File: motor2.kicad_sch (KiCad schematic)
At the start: 58 parts, among them IC3 DRV8300DPWR, IC4 DRV8300DPWR, J1 Conn_01x01, J2 Conn_01x01, J3 Conn_01x01, J4 Conn_01x01, J5 Conn_01x01, J6 Conn_01x01, Q1 Q_NMOS, Q10 Q_NMOS, Q11 Q_NMOS, Q12 Q_NMOS, Q2 Q_NMOS, Q3 Q_NMOS, Q4 Q_NMOS, Q5 Q_NMOS, Q6 Q_NMOS, Q7 Q_NMOS, Q8 Q_NMOS, Q9 Q_NMOS

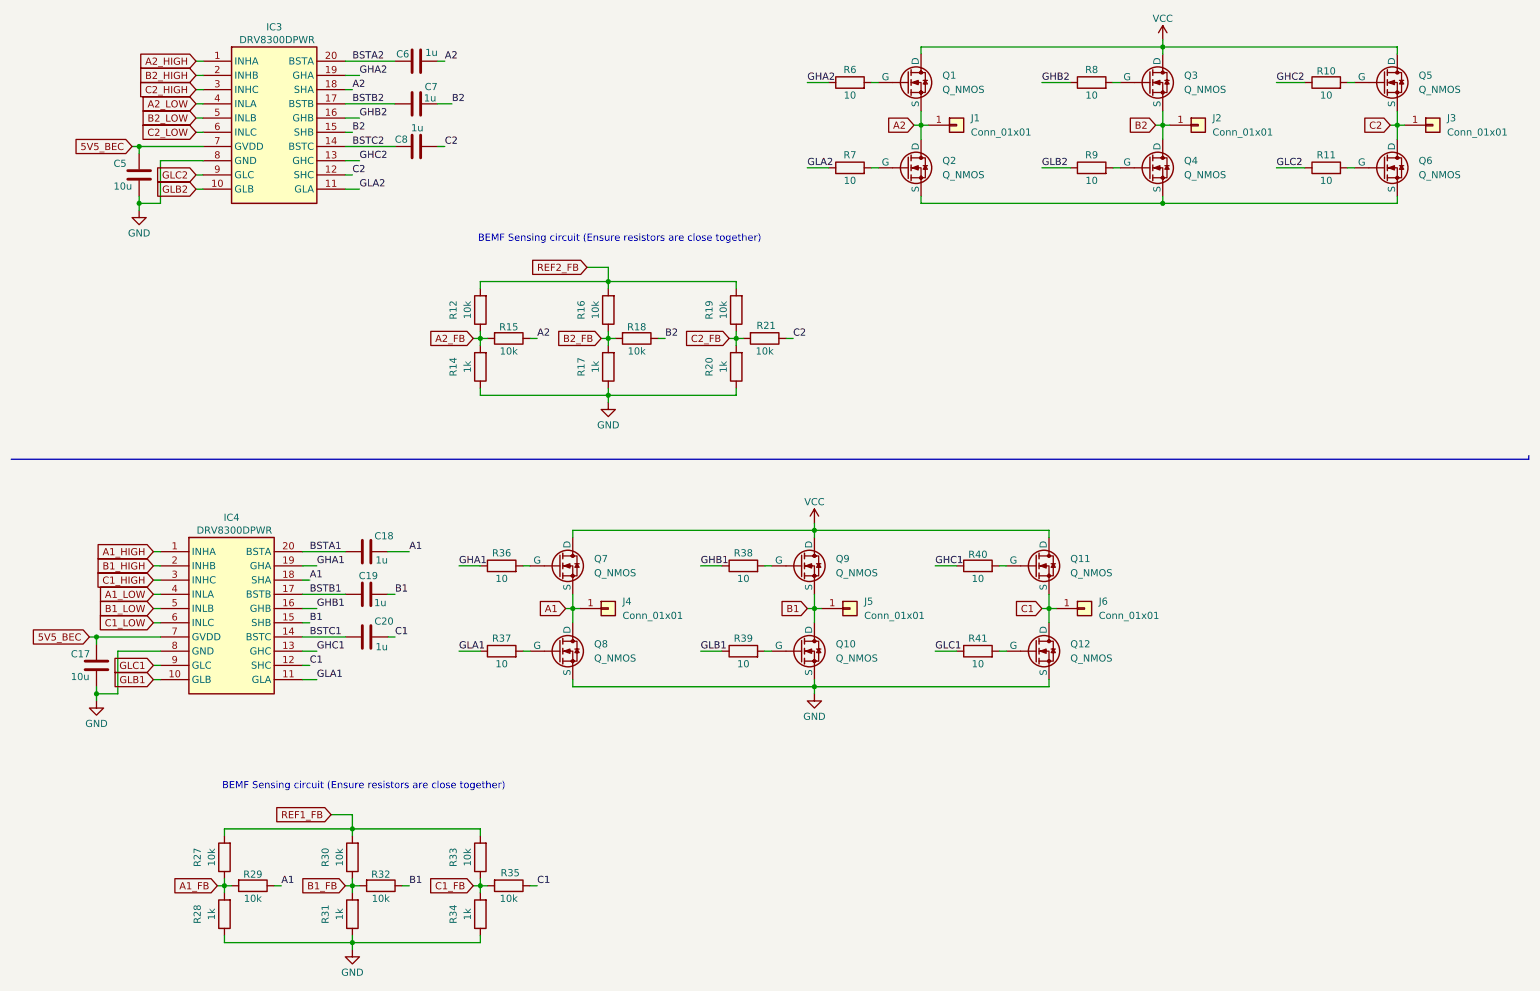
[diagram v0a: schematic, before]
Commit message: update schematic
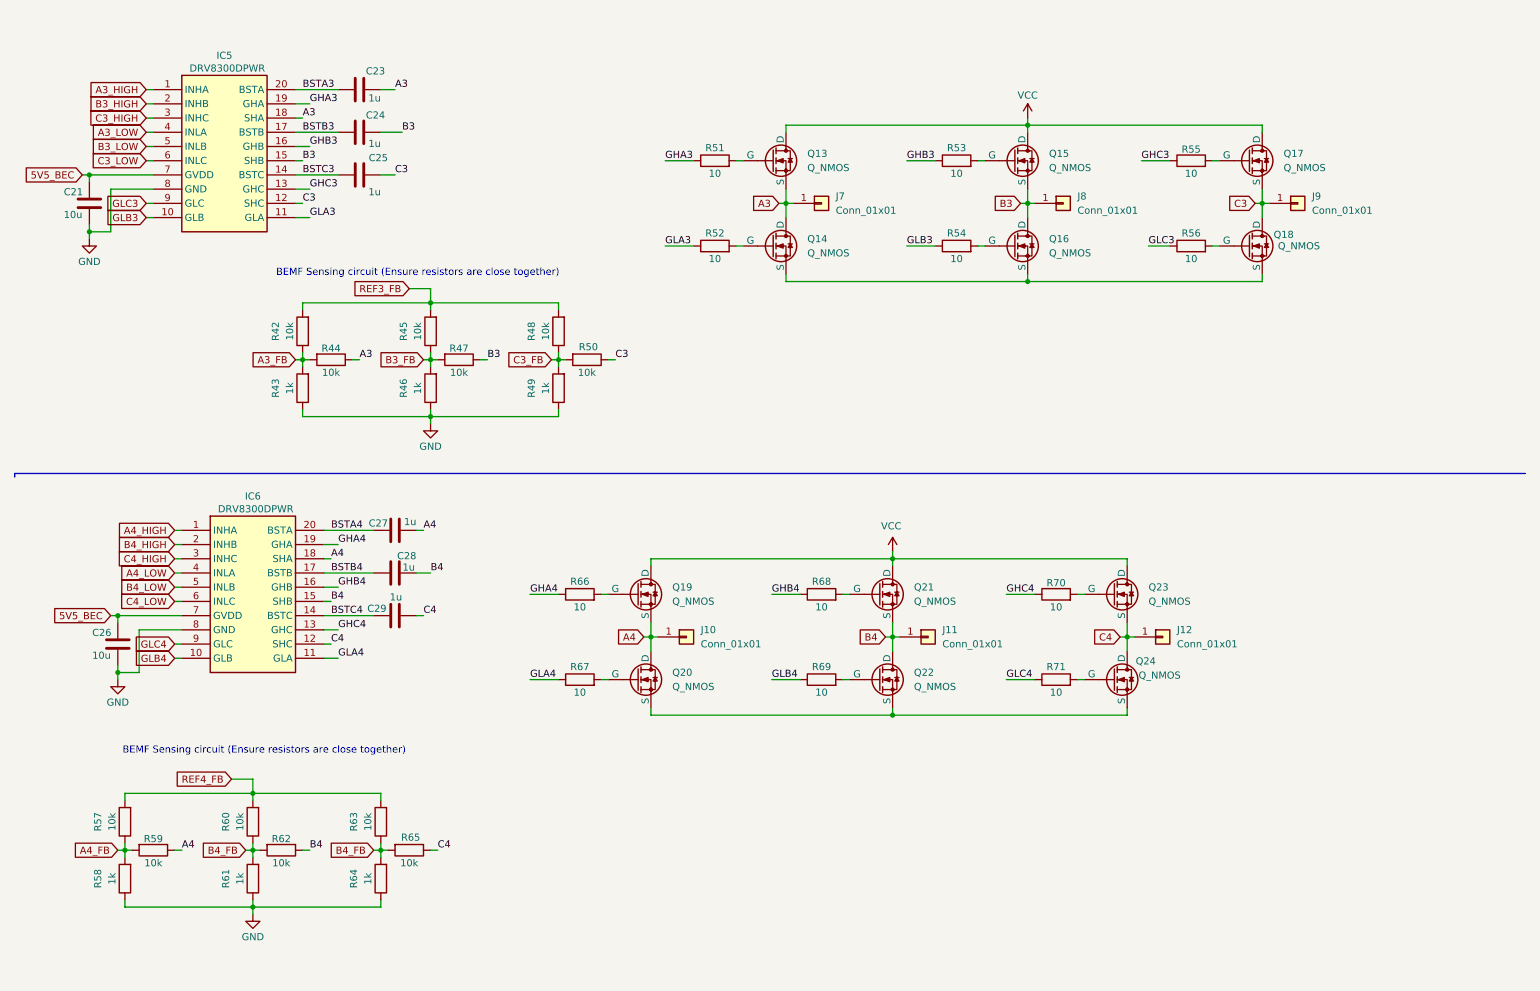
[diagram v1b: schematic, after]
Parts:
- removed C17, C5: 10u, symbol Device:C
- removed C18, C19, C20, C6, C7, C8: 1u, symbol Device:C
- removed IC3, IC4: DRV8300DPWR, ESCs:SOP65P640X120-20M, symbol ESCs:DRV8300DPWR
- removed J1, J2, J3, J4, J5, J6: Conn_01x01, symbol Connector_Generic:Conn_01x01
- removed Q1, Q10, Q11, Q12, Q2, Q3, Q4, Q5, Q6, Q7, Q8, Q9: Q_NMOS, symbol Device:Q_NMOS
- removed R10, R11, R36, R37, R38, R39, R40, R41, R6, R7, R8, R9: 10, symbol Device:R
- removed R12, R15, R16, R18, R19, R21, R27, R29, R30, R32, R33, R35: 10k, symbol Device:R
- removed R14, R17, R20, R28, R31, R34: 1k, symbol Device:R
- added C21, C26: 10u, symbol Device:C
- added C23, C24, C25, C27, C28, C29: 1u, symbol Device:C
- added IC5, IC6: DRV8300DPWR, ESCs:SOP65P640X120-20M, symbol ESCs:DRV8300DPWR
- added J10, J11, J12, J7, J8, J9: Conn_01x01, symbol Connector_Generic:Conn_01x01
- added Q13, Q14, Q15, Q16, Q17, Q18, Q19, Q20, Q21, Q22, Q23, Q24: Q_NMOS, symbol Device:Q_NMOS
- added R42, R44, R45, R47, R48, R50, R57, R59, R60, R62, R63, R65: 10k, symbol Device:R
- added R43, R46, R49, R58, R61, R64: 1k, symbol Device:R
- added R51, R52, R53, R54, R55, R56, R66, R67, R68, R69, R70, R71: 10, symbol Device:R
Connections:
- net 5V5_BEC: now also C21.1, C26.1, IC5.7 (GVDD), IC6.7 (GVDD)
- net GND: now also C21.2, C26.2, IC5.8 (GND), IC6.8 (GND), R43.1, R46.1, R49.1, R58.1, R61.1, R64.1
- net VCC: now also Q13.D, Q15.D, Q17.D, Q19.D, Q21.D, Q23.D
- new net: Q15.G, R53.2
- new net: Q20.G, R67.2
- new net: Q20.S, Q22.S, Q24.S
- new net: Q19.G, R66.2
- new net: Q22.G, R69.2
- new net: Q23.G, R70.2
- new net: Q24.G, R71.2
- new net: Q17.G, R55.2
- new net: Q21.G, R68.2
- new net: Q13.G, R51.2
- new net: Q14.G, R52.2
- new net: Q14.S, Q16.S, Q18.S
- new net: Q18.G, R56.2
- new net: Q16.G, R54.2
- new net A3: C23.2, IC5.18 (SHA), J7.1 (Pin_1), Q13.S, Q14.D, R44.1
- new net A3_FB: R42.1, R43.2, R44.2
- new net A3_HIGH: IC5.1 (INHA)
- new net A3_LOW: IC5.4 (INLA)
- new net A4: C27.2, IC6.18 (SHA), J10.1 (Pin_1), Q19.S, Q20.D, R59.1
- new net A4_FB: R57.1, R58.2, R59.2
- new net A4_HIGH: IC6.1 (INHA)
- new net A4_LOW: IC6.4 (INLA)
- new net B3: C24.2, IC5.15 (SHB), J8.1 (Pin_1), Q15.S, Q16.D, R47.1
- new net B3_FB: R45.1, R46.2, R47.2
- new net B3_HIGH: IC5.2 (INHB)
- new net B3_LOW: IC5.5 (INLB)
- new net B4: C28.2, IC6.15 (SHB), J11.1 (Pin_1), Q21.S, Q22.D, R62.1
- new net B4_FB: R60.1, R61.2, R62.2, R63.1, R64.2, R65.2
- new net B4_HIGH: IC6.2 (INHB)
- new net B4_LOW: IC6.5 (INLB)
- new net BSTA3: C23.1, IC5.20 (BSTA)
- new net BSTA4: C27.1, IC6.20 (BSTA)
- new net BSTB3: C24.1, IC5.17 (BSTB)
- new net BSTB4: C28.1, IC6.17 (BSTB)
- new net BSTC3: C25.1, IC5.14 (BSTC)
- new net BSTC4: C29.1, IC6.14 (BSTC)
- new net C3: C25.2, IC5.12 (SHC), J9.1 (Pin_1), Q17.S, Q18.D, R50.1
- new net C3_FB: R48.1, R49.2, R50.2
- new net C3_HIGH: IC5.3 (INHC)
- new net C3_LOW: IC5.6 (INLC)
- new net C4: C29.2, IC6.12 (SHC), J12.1 (Pin_1), Q23.S, Q24.D, R65.1
- new net C4_HIGH: IC6.3 (INHC)
- new net C4_LOW: IC6.6 (INLC)
- new net GHA3: IC5.19 (GHA), R51.1
- new net GHA4: IC6.19 (GHA), R66.1
- new net GHB3: IC5.16 (GHB), R53.1
- new net GHB4: IC6.16 (GHB), R68.1
- new net GHC3: IC5.13 (GHC), R55.1
- new net GHC4: IC6.13 (GHC), R70.1
- new net GLA3: IC5.11 (GLA), R52.1
- new net GLA4: IC6.11 (GLA), R67.1
- new net GLB3: IC5.10 (GLB), R54.1
- new net GLB4: IC6.10 (GLB), R69.1
- new net GLC3: IC5.9 (GLC), R56.1
- new net GLC4: IC6.9 (GLC), R71.1
- new net REF3_FB: R42.2, R45.2, R48.2
- new net REF4_FB: R57.2, R60.2, R63.2

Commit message: affected footprints
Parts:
- C21, C23, C24, C25, C26, C27, C28, C29: footprint (none) -> Capacitor_SMD:C_0402_1005Metric
- J10, J11, J12, J7, J8, J9: footprint (none) -> TestPoint:TestPoint_Pad_2.0x2.0mm; now left out of the parts list
- Q13, Q14, Q15, Q16, Q17, Q18, Q19, Q20, Q21, Q22, Q23, Q24: footprint (none) -> ESCs:TRANS_NTMFS5C628NLT1G
- R42, R43, R44, R45, R46, R47, R48, R49, R50, R51, R52, R53, R54, R55, R56, R57, R58, R59, R60, R61, R62, R63, R64, R65, R66, R67, R68, R69, R70, R71: footprint (none) -> Resistor_SMD:R_0402_1005Metric
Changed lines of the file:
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@@
 			)
 		)
-		(property "Footprint" ""
+		(property "Footprint" "Resistor_SMD:R_0402_1005Metric"
 			(at 181.61 42.418 90)
 			(effects
@@
 			)
 		)
-		(property "Footprint" ""
+		(property "Footprint" "ESCs:TRANS_NTMFS5C628NLT1G"
 			(at 129.54 130.81 0)
 			(effects
@@
 			)
 		)
-		(property "Footprint" ""
+		(property "Footprint" "ESCs:TRANS_NTMFS5C628NLT1G"
 			(at 129.54 115.57 0)
 			(effects
@@
 			)
 		)
-		(property "Footprint" ""
+		(property "Footprint" "Resistor_SMD:R_0402_1005Metric"
 			(at 66.548 71.12 90)
 			(effects
@@
 			)
 		)
-		(property "Footprint" ""
+		(property "Footprint" "Resistor_SMD:R_0402_1005Metric"
 			(at 112.268 81.28 90)
 			(effects
@@
 			)
 		)
-		(property "Footprint" ""
+		(property "Footprint" "Resistor_SMD:R_0402_1005Metric"
 			(at 157.48 135.128 90)
 			(effects
@@
 			)
 		)
-		(property "Footprint" ""
+		(property "Footprint" "Resistor_SMD:R_0402_1005Metric"
 			(at 199.39 119.888 90)
 			(effects
@@
 			)
 		)
-		(property "Footprint" ""
+		(property "Footprint" "ESCs:TRANS_NTMFS5C628NLT1G"
 			(at 214.63 115.57 0)
 			(effects
@@
 			)
 		)
-		(property "Footprint" ""
+		(property "Footprint" "Resistor_SMD:R_0402_1005Metric"
 			(at 57.658 158.75 90)
 			(effects
@@
 			)
 		)
-		(property "Footprint" ""
+		(property "Footprint" "Resistor_SMD:R_0402_1005Metric"
 			(at 38.1 162.052 90)
 			(effects
@@
 			)
 		)
-		(property "Footprint" ""
+		(property "Footprint" "ESCs:TRANS_NTMFS5C628NLT1G"
 			(at 214.63 130.81 0)
 			(effects
@@
 		(unit 1)
 		(exclude_from_sim no)
-		(in_bom yes)
+		(in_bom no)
 		(on_board yes)
 		(dnp no)
@@
 			)
 		)
-		(property "Footprint" ""
+		(property "Footprint" "TestPoint:TestPoint_Pad_2.0x2.0mm"
 			(at 176.53 125.73 0)
 			(effects
@@
 			)
 		)
-		(property "Footprint" ""
+		(property "Footprint" "Resistor_SMD:R_0402_1005Metric"
 			(at 34.798 158.75 90)
 			(effects
@@
 			)
 		)
-		(property "Footprint" ""
+		(property "Footprint" "Capacitor_SMD:C_0402_1005Metric"
 			(at 85.09 105.7148 0)
 			(effects
@@
 			)
 		)
-		(property "Footprint" ""
+		(property "Footprint" "Capacitor_SMD:C_0402_1005Metric"
 			(at 85.09 113.3348 0)
 			(effects
@@
 			)
 		)
-		(property "Footprint" ""
+		(property "Footprint" "ESCs:TRANS_NTMFS5C628NLT1G"
 			(at 238.76 38.1 0)
 			(effects
@@
 			)
 		)
-		(property "Footprint" ""
+		(property "Footprint" "Resistor_SMD:R_0402_1005Metric"
 			(at 115.57 74.422 90)
 			(effects
@@
 		(unit 1)
 		(exclude_from_sim no)
-		(in_bom yes)
+		(in_bom no)
 		(on_board yes)
 		(dnp no)
@@
 			)
 		)
-		(property "Footprint" ""
+		(property "Footprint" "TestPoint:TestPoint_Pad_2.0x2.0mm"
 			(at 200.66 48.26 0)
 			(effects
@@
 			)
 		)
-		(property "Footprint" ""
+		(property "Footprint" "Resistor_SMD:R_0402_1005Metric"
 			(at 60.96 162.052 90)
 			(effects
@@
 		(unit 1)
 		(exclude_from_sim no)
-		(in_bom yes)
+		(in_bom no)
 		(on_board yes)
 		(dnp no)
@@
 			)
 		)
-		(property "Footprint" ""
+		(property "Footprint" "TestPoint:TestPoint_Pad_2.0x2.0mm"
 			(at 133.35 125.73 0)
 			(effects
@@
 		(unit 1)
 		(exclude_from_sim no)
-		(in_bom yes)
+		(in_bom no)
 		(on_board yes)
 		(dnp no)
@@
 			)
 		)
-		(property "Footprint" ""
+		(property "Footprint" "TestPoint:TestPoint_Pad_2.0x2.0mm"
 			(at 218.44 125.73 0)
 			(effects
@@
 			)
 		)
-		(property "Footprint" ""
+		(property "Footprint" "Resistor_SMD:R_0402_1005Metric"
 			(at 157.48 119.888 90)
 			(effects
@@
 			)
 		)
-		(property "Footprint" ""
+		(property "Footprint" "ESCs:TRANS_NTMFS5C628NLT1G"
 			(at 153.67 38.1 0)
 			(effects
@@
 			)
 		)
-		(property "Footprint" ""
+		(property "Footprint" "Resistor_SMD:R_0402_1005Metric"
 			(at 57.658 168.91 90)
 			(effects
@@
 			)
 		)
-		(property "Footprint" ""
+		(property "Footprint" "Resistor_SMD:R_0402_1005Metric"
 			(at 138.43 42.418 90)
 			(effects
@@
 			)
 		)
-		(property "Footprint" ""
+		(property "Footprint" "Resistor_SMD:R_0402_1005Metric"
 			(at 80.518 168.91 90)
 			(effects
@@
 			)
 		)
-		(property "Footprint" ""
+		(property "Footprint" "Resistor_SMD:R_0402_1005Metric"
 			(at 114.3 135.128 90)
 			(effects
@@
 			)
 		)
-		(property "Footprint" ""
+		(property "Footprint" "Resistor_SMD:R_0402_1005Metric"
 			(at 89.408 81.28 90)
 			(effects
@@
 			)
 		)
-		(property "Footprint" ""
+		(property "Footprint" "ESCs:TRANS_NTMFS5C628NLT1G"
 			(at 153.67 53.34 0)
 			(effects
@@
 			)
 		)
-		(property "Footprint" ""
+		(property "Footprint" "Resistor_SMD:R_0402_1005Metric"
 			(at 112.268 71.12 90)
 			(effects
@@
 		(unit 1)
 		(exclude_from_sim no)
-		(in_bom yes)
+		(in_bom no)
 		(on_board yes)
 		(dnp no)
@@
 			)
 		)
-		(property "Footprint" ""
+		(property "Footprint" "TestPoint:TestPoint_Pad_2.0x2.0mm"
 			(at 157.48 48.26 0)
 			(effects
@@
 			)
 		)
-		(property "Footprint" ""
+		(property "Footprint" "ESCs:TRANS_NTMFS5C628NLT1G"
 			(at 238.76 53.34 0)
 			(effects
@@
 			)
 		)
-		(property "Footprint" ""
+		(property "Footprint" "Resistor_SMD:R_0402_1005Metric"
 			(at 223.52 42.418 90)
 			(effects
@@
 			)
 		)
-		(property "Footprint" ""
+		(property "Footprint" "ESCs:TRANS_NTMFS5C628NLT1G"
 			(at 196.85 38.1 0)
 			(effects
@@
 			)
 		)
-		(property "Footprint" ""
+		(property "Footprint" "Resistor_SMD:R_0402_1005Metric"
 			(at 34.798 168.91 90)
 			(effects
@@
 			)
 		)
-		(property "Footprint" ""
+		(property "Footprint" "Resistor_SMD:R_0402_1005Metric"
 			(at 138.43 57.658 90)
 			(effects
@@
 			)
 		)
-		(property "Footprint" ""
+		(property "Footprint" "Resistor_SMD:R_0402_1005Metric"
 			(at 89.408 71.12 90)
 			(effects
@@
 			)
 		)
-		(property "Footprint" ""
+		(property "Footprint" "Resistor_SMD:R_0402_1005Metric"
 			(at 66.548 81.28 90)
 			(effects
@@
 			)
 		)
-		(property "Footprint" ""
+		(property "Footprint" "Capacitor_SMD:C_0402_1005Metric"
 			(at 78.74 26.9748 0)
 			(effects
@@
 			)
 		)
-		(property "Footprint" ""
+		(property "Footprint" "Capacitor_SMD:C_0402_1005Metric"
 			(at 78.74 42.2148 0)
 			(effects
@@
 			)
 		)
-		(property "Footprint" ""
+		(property "Footprint" "Capacitor_SMD:C_0402_1005Metric"
 			(at 78.74 34.5948 0)
 			(effects
@@
 			)
 		)
-		(property "Footprint" ""
+		(property "Footprint" "ESCs:TRANS_NTMFS5C628NLT1G"
 			(at 172.72 130.81 0)
 			(effects
@@
 			)
 		)
-		(property "Footprint" ""
+		(property "Footprint" "ESCs:TRANS_NTMFS5C628NLT1G"
 			(at 196.85 53.34 0)
 			(effects
@@
 			)
 		)
-		(property "Footprint" ""
+		(property "Footprint" "Capacitor_SMD:C_0402_1005Metric"
 			(at 27.6352 52.07 0)
 			(effects
@@
 			)
 		)
-		(property "Footprint" ""
+		(property "Footprint" "Resistor_SMD:R_0402_1005Metric"
 			(at 80.518 158.75 90)
 			(effects
@@
 			)
 		)
-		(property "Footprint" ""
+		(property "Footprint" "Capacitor_SMD:C_0402_1005Metric"
 			(at 32.7152 130.81 0)
 			(effects
@@
 			)
 		)
-		(property "Footprint" ""
+		(property "Footprint" "ESCs:TRANS_NTMFS5C628NLT1G"
 			(at 172.72 115.57 0)
 			(effects
@@
 			)
 		)
-		(property "Footprint" ""
+		(property "Footprint" "Resistor_SMD:R_0402_1005Metric"
 			(at 83.82 162.052 90)
 			(effects
@@
 		(unit 1)
 		(exclude_from_sim no)
-		(in_bom yes)
+		(in_bom no)
 		(on_board yes)
 		(dnp no)
@@
 			)
 		)
-		(property "Footprint" ""
+		(property "Footprint" "TestPoint:TestPoint_Pad_2.0x2.0mm"
 			(at 242.57 48.26 0)
 			(effects
@@
 			)
 		)
-		(property "Footprint" ""
+		(property "Footprint" "Resistor_SMD:R_0402_1005Metric"
 			(at 114.3 119.888 90)
 			(effects
@@
 			)
 		)
-		(property "Footprint" ""
+		(property "Footprint" "Resistor_SMD:R_0402_1005Metric"
 			(at 92.71 74.422 90)
 			(effects
@@
 			)
 		)
-		(property "Footprint" ""
+		(property "Footprint" "Capacitor_SMD:C_0402_1005Metric"
 			(at 85.09 120.9548 0)
 			(effects
@@
 			)
 		)
-		(property "Footprint" ""
+		(property "Footprint" "Resistor_SMD:R_0402_1005Metric"
 			(at 69.85 74.422 90)
 			(effects
@@
 			)
 		)
-		(property "Footprint" ""
+		(property "Footprint" "Resistor_SMD:R_0402_1005Metric"
 			(at 181.61 57.658 90)
 			(effects
@@
 			)
 		)
-		(property "Footprint" ""
+		(property "Footprint" "Resistor_SMD:R_0402_1005Metric"
 			(at 199.39 135.128 90)
 			(effects
@@
 			)
 		)
-		(property "Footprint" ""
+		(property "Footprint" "Resistor_SMD:R_0402_1005Metric"
 			(at 223.52 57.658 90)
 			(effects

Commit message: minor fixes
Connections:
- net GHB3_R: now reaches Q15.G, R53.2
- net GLA4_R: now reaches Q20.G, R67.2
- net GHA4_R: now reaches Q19.G, R66.2
- net GLB4_R: now reaches Q22.G, R69.2
- net GHC4_R: now reaches Q23.G, R70.2
- net GLC4_R: now reaches Q24.G, R71.2
- net GHC3_R: now reaches Q17.G, R55.2
- net GHB4_R: now reaches Q21.G, R68.2
- net GHA3_R: now reaches Q13.G, R51.2
- net GLA3_R: now reaches Q14.G, R52.2
- net GLC3_R: now reaches Q18.G, R56.2
- net GLB3_R: now reaches Q16.G, R54.2
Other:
- moved on the sheet: J10, J11, J12, J7, J8, J9, Q13, Q14, Q15, Q16, Q17, Q18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
